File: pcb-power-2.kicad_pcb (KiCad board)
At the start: 2 copper layers, 30 x 58 mm, 23 parts, among them J1 Conn_01x04_Socket, J12 Conn_01x02_Socket, J2 Conn_01x02_Socket, J3 Conn_01x02_Socket, J4 Conn_01x02_Socket, J5 Conn_01x03_Socket, Q2 NMOS, Q4 PMOS, U1 LM1117DT-5.0, U2 IRF7303, U3 LM1117DT-5.0, U4 IRF7104

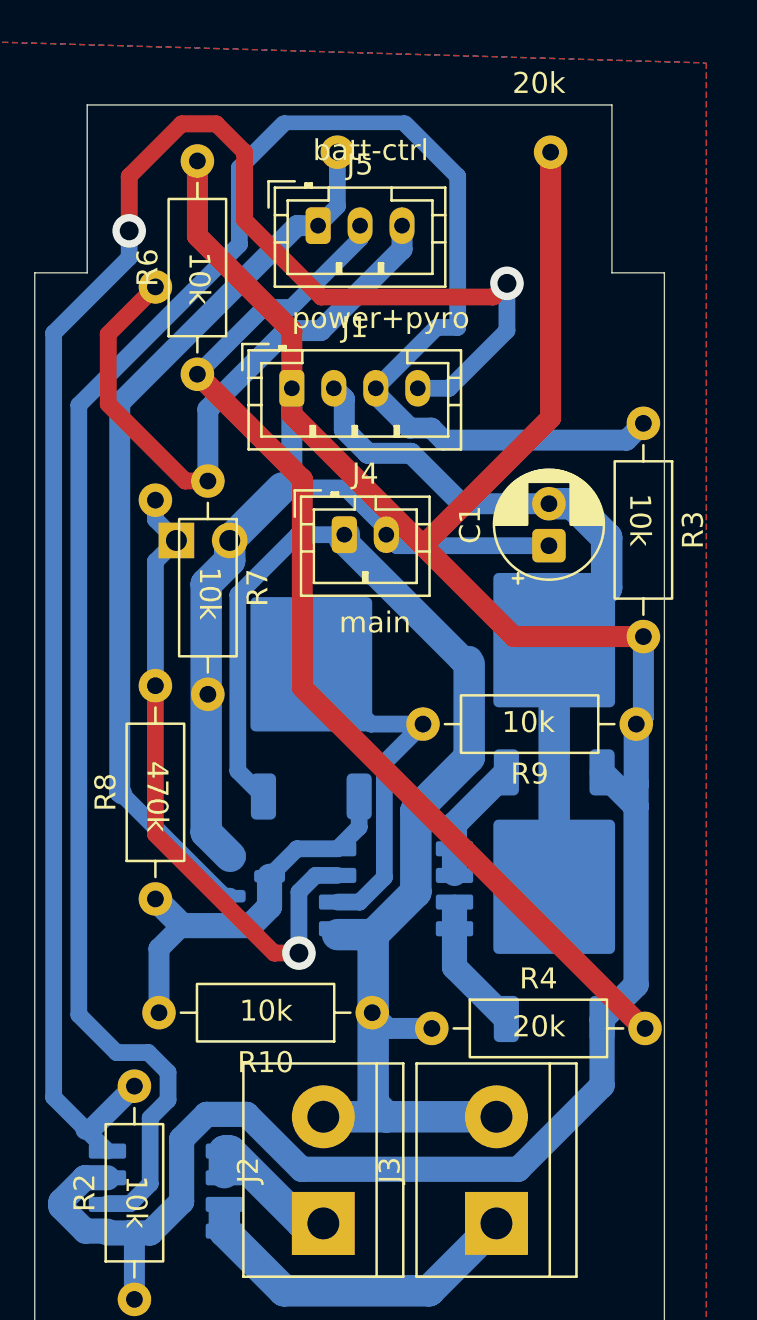
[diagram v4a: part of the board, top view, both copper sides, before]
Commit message: Fixed silkscreen
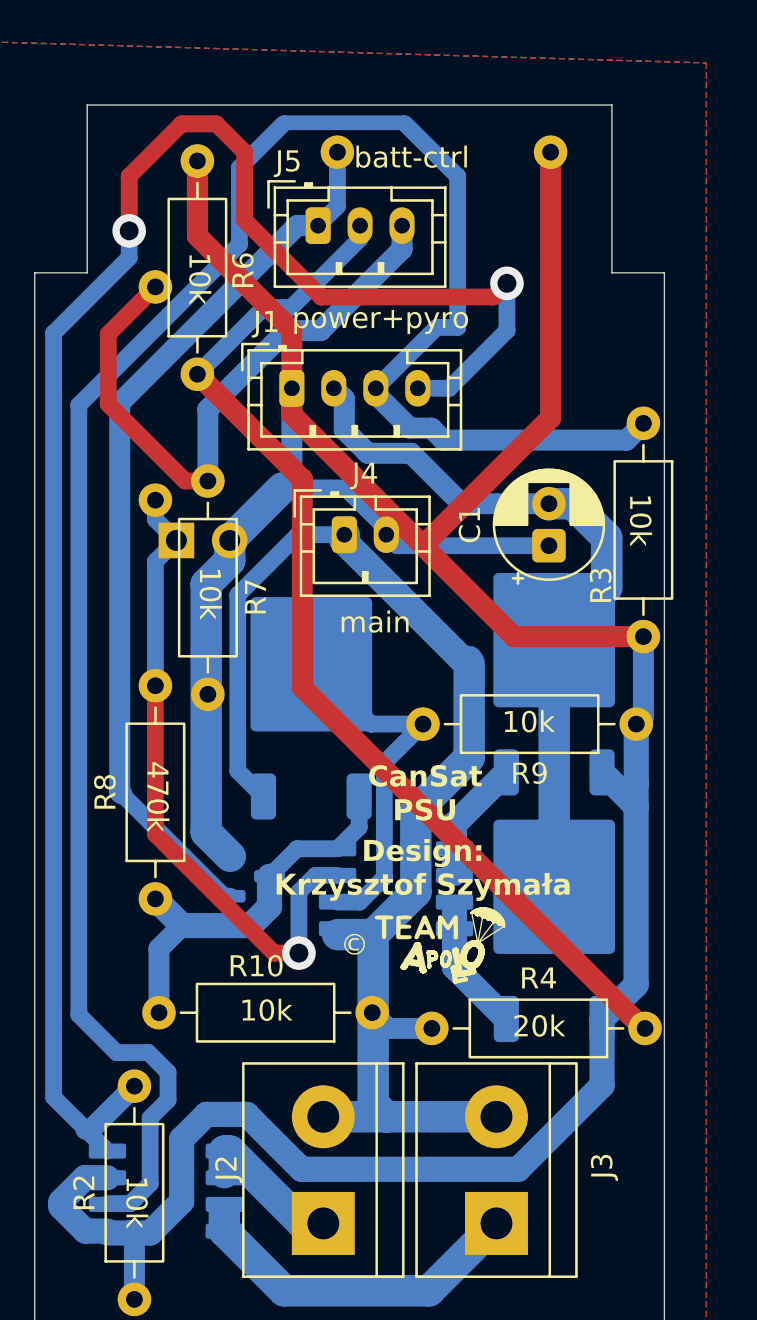
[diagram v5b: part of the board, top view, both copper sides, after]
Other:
- board text added: "CanSat PSU"
- board text added: "Design: Krzysztof Szymała"
- board text added: "©"
